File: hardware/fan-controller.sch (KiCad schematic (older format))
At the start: 60 parts

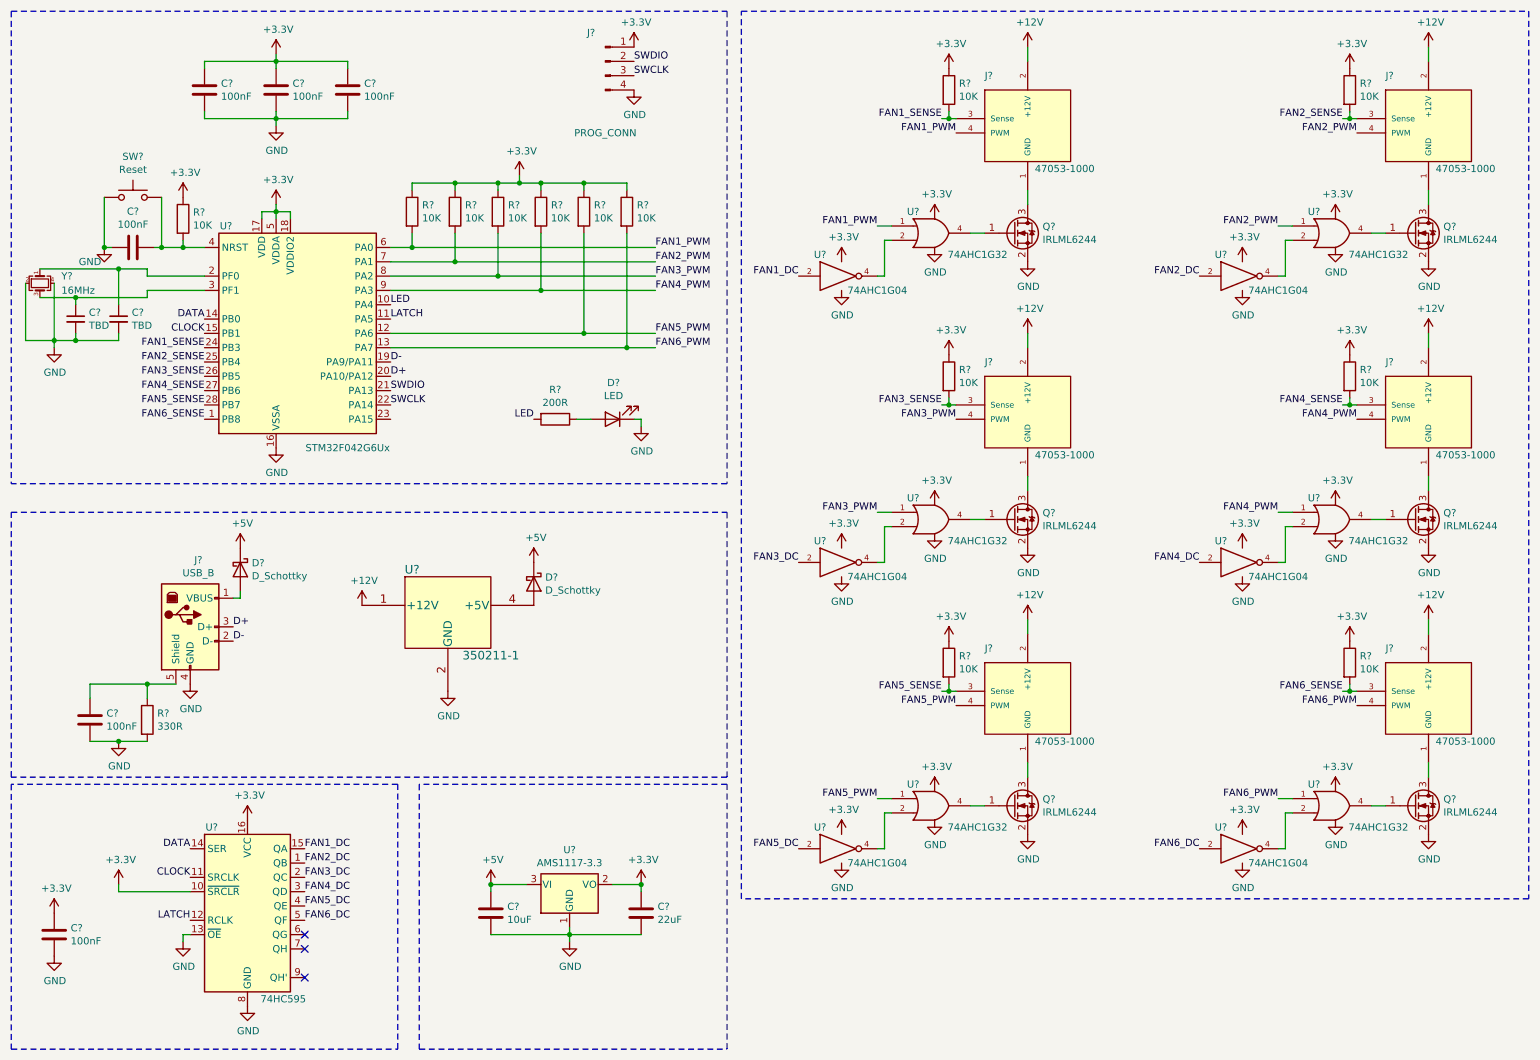
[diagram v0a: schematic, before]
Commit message: Done PCB, changed schematic a bit
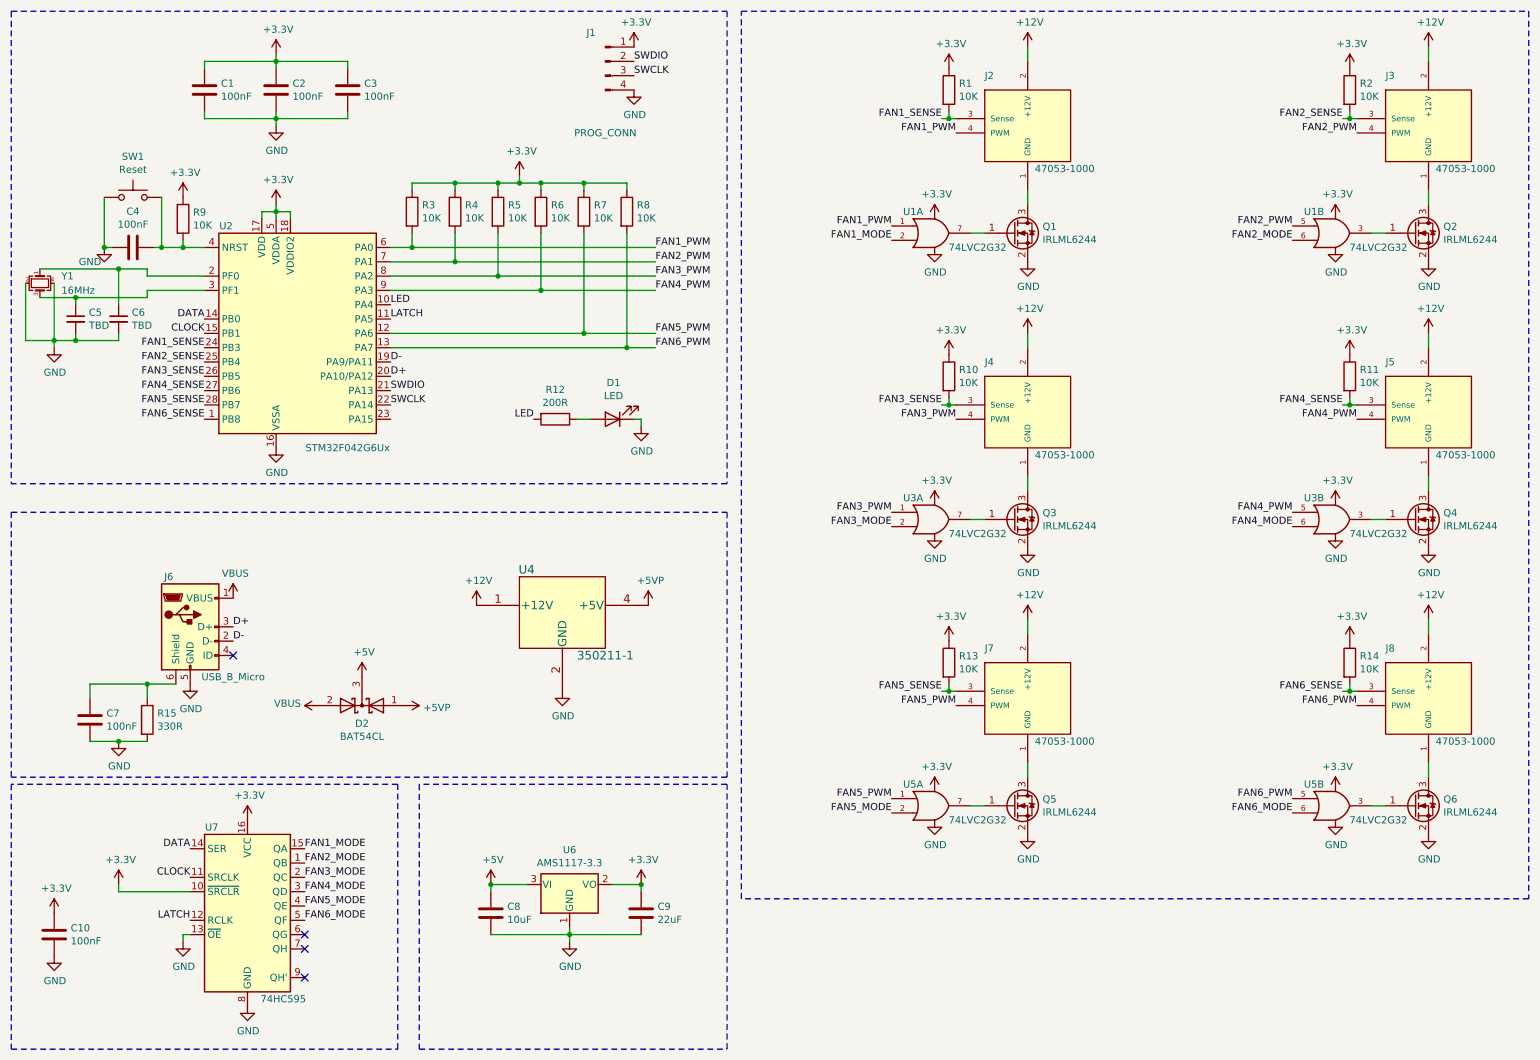
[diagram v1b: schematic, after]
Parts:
- removed D? (x2): D_Schottky, symbol Device:D_Schottky
- removed J?: USB_B, symbol Connector:USB_B
- removed U? (x6): 74AHC1G32, symbol 74xGxx:74AHC1G32
- removed U? (x6): 74AHC1G04, symbol 74xGxx:74AHC1G04
- added D2: BAT54CL, Package_TO_SOT_SMD:SOT-23_Handsoldering, symbol Device:D_Schottky_x2_KCom_AAK
- added J6: USB_B_Micro, Connector_USB:USB_Micro-B_Molex-105017-0001, symbol Connector:USB_B_Micro
- added U1, U3, U5: 74LVC2G32, Package_SO:VSSOP-8_2.3x2mm_P0.5mm, symbol 74xGxx:74LVC2G32
- C1, C10, C2, C3, C4, C5, C6, C7: renamed from C?; footprint (none) -> Capacitor_SMD:C_0805_2012Metric_Pad1.18x1.45mm_HandSolder
- C8, C9: renamed from C?; footprint (none) -> Capacitor_SMD:C_1206_3216Metric_Pad1.33x1.80mm_HandSolder
- D1: renamed from D?; footprint (none) -> LED_SMD:LED_1206_3216Metric_Pad1.42x1.75mm_HandSolder
- J1: renamed from J?; footprint (none) -> Connector_PinHeader_2.54mm:PinHeader_1x04_P2.54mm_Vertical
- R1, R10, R11, R12, R13, R14, R15, R2, R3, R4, R5, R6, R7, R8, R9: renamed from R?; footprint (none) -> Resistor_SMD:R_0805_2012Metric_Pad1.20x1.40mm_HandSolder
- SW1: renamed from SW?; footprint (none) -> TS-1187A-B-A-B:SW_TS-1187A-B-A-B
- U7: renamed from U?; footprint (none) -> Package_SO:SOIC-16_3.9x9.9mm_P1.27mm
- Y1: renamed from Y?; footprint (none) -> Crystal:Crystal_SMD_2520-4Pin_2.5x2.0mm
- gave numbers to parts that had none: 15
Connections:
- net +3V3: now also U1.8 (VCC), U1.8 (VCC), U3.8 (VCC), U3.8 (VCC), U5.8 (VCC), U5.8 (VCC)
- net +5V: now also D2.3 (K)
- net D+: now also J6.3 (D+)
- net D-: now also J6.2 (D-)
- net FAN1_PWM: now also U1.1
- net FAN2_PWM: now also U1.5
- net FAN3_PWM: now also U3.1
- net FAN4_PWM: now also U3.5
- net FAN5_PWM: now also U5.1
- net FAN6_PWM: now also U5.5
- net GND: now also J6.5 (GND), U1.4 (GND), U1.4 (GND), U3.4 (GND), U3.4 (GND), U5.4 (GND), U5.4 (GND)
- net +5VP: now reaches U4.4 (+5V)
- net +5VP: now also D2.1 (A)
- net at C7.1, R15.1: now also J6.6 (Shield)
- net at Q5.1 (G): now also U5.7
- net at Q3.1 (G): now also U3.7
- net at Q4.1 (G): now also U3.3
- net at Q6.1 (G): now also U5.3
- net at Q2.1 (G): now also U1.3
- net at Q1.1 (G): now also U1.7
- net FAN1_DC renamed FAN1_MODE
- net FAN1_MODE: now also U1.2
- net FAN2_DC renamed FAN2_MODE
- net FAN2_MODE: now also U1.6
- net FAN3_DC renamed FAN3_MODE
- net FAN3_MODE: now also U3.2
- net FAN4_DC renamed FAN4_MODE
- net FAN4_MODE: now also U3.6
- net FAN5_DC renamed FAN5_MODE
- net FAN5_MODE: now also U5.2
- net FAN6_DC renamed FAN6_MODE
- net FAN6_MODE: now also U5.6
- new net VBUS: D2.2 (A), J6.1 (VBUS)
- no-connect marks 3 -> 4
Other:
- moved on the sheet: U4
